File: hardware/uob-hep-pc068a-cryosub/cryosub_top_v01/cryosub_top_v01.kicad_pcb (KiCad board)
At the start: 2 copper layers, 146.8 x 25 mm, 44 parts, among them J1 Conn_02x05_Top_Bottom, J2 Conn_01x04_Male, Q1 BSS127S, Q2 BSS127S, Q3 FDD306P, Q4 BSS127S, Q5 BSS127S, Q6 FDD306P, U1 CMOD-A7

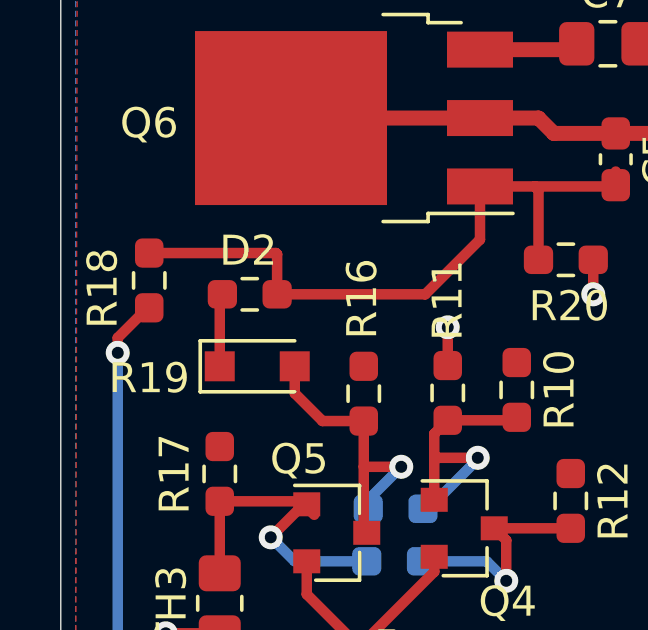
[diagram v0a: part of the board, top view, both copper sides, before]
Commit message: Tuning simulation to change on/off temperature. Then making the resulting changes to BoM
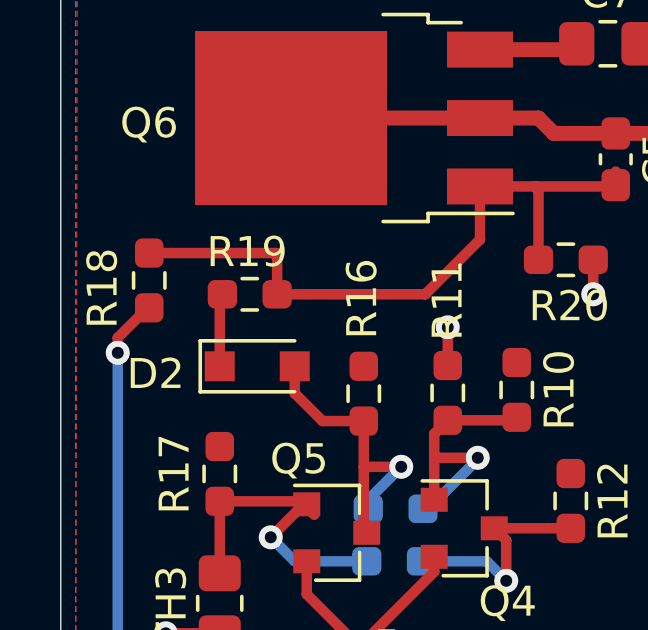
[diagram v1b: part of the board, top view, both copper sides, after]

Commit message: Updated BoM, correctly this time I hope, to update resistor values for correct set-points
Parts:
- R1, R8: value 6.6k -> 62k
- R10, R17: value 6.6k -> 6.8k
- R2: value 10k -> 100k
- R4, R6: value 10k -> 200k
